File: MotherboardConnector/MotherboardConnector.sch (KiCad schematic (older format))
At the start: 2 parts

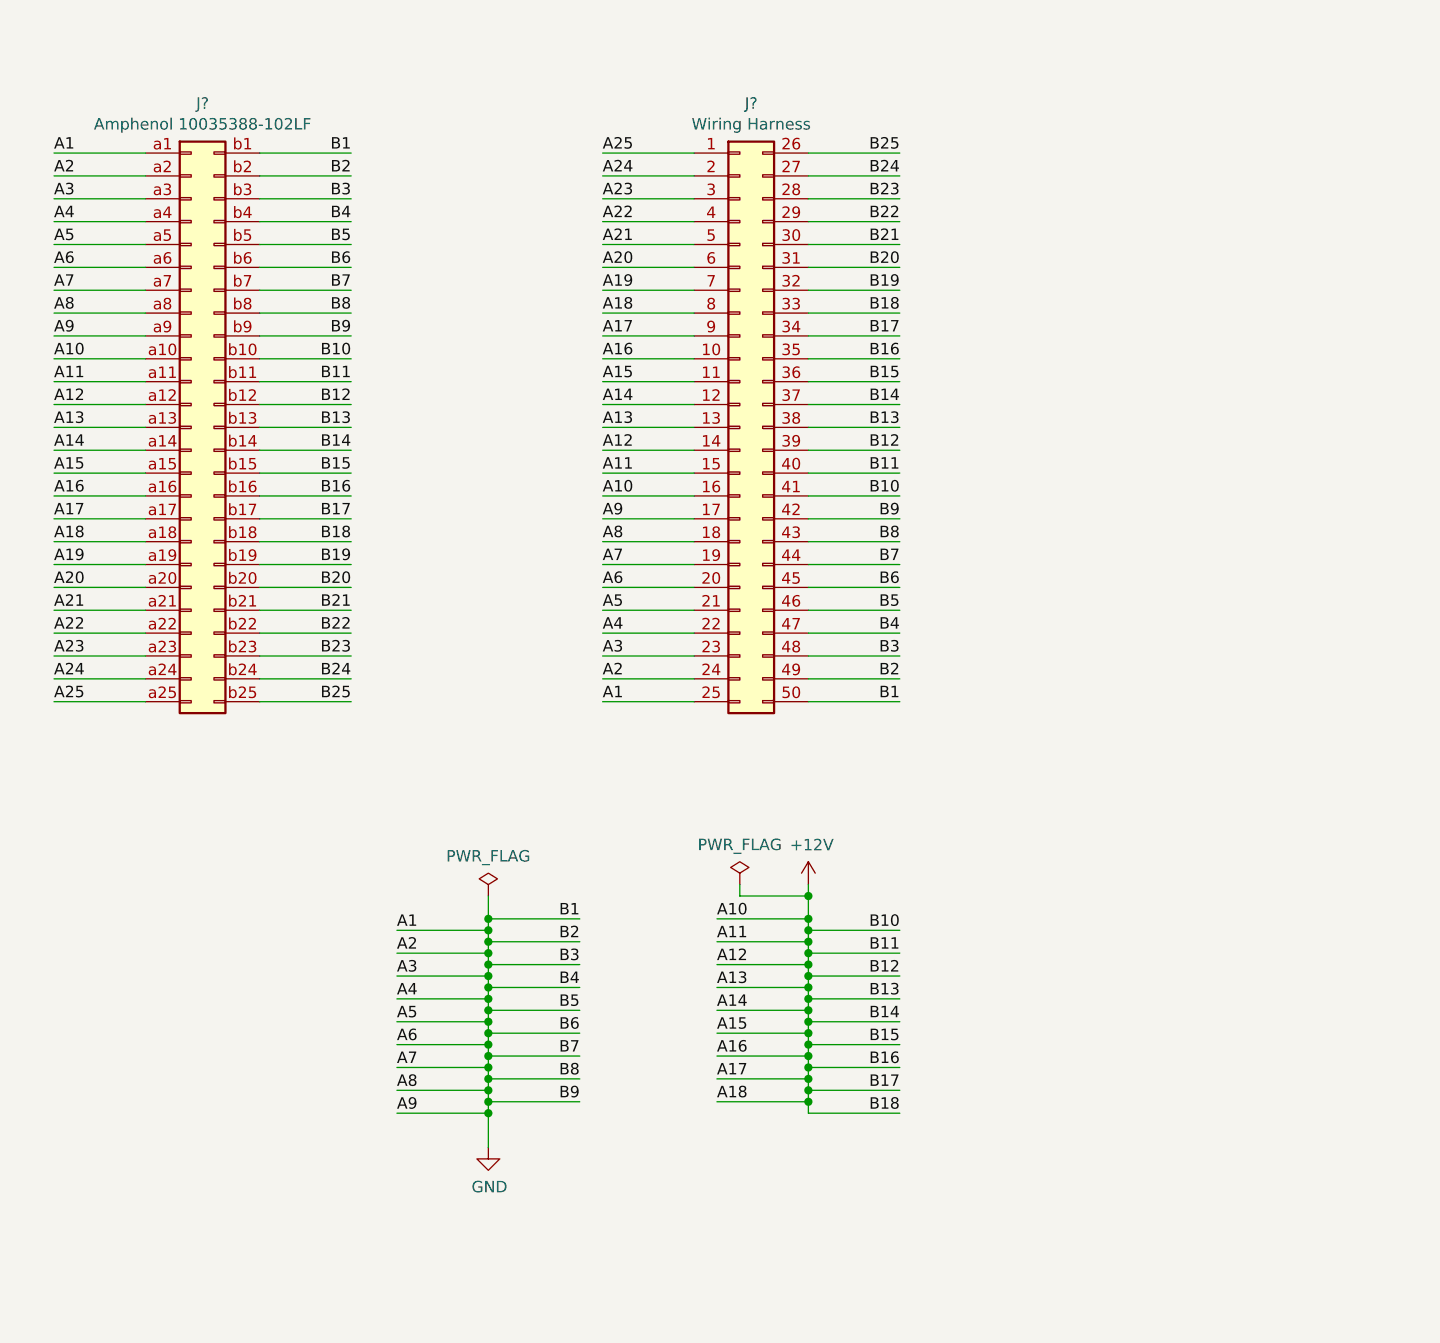
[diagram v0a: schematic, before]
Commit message: change to terminal block connector
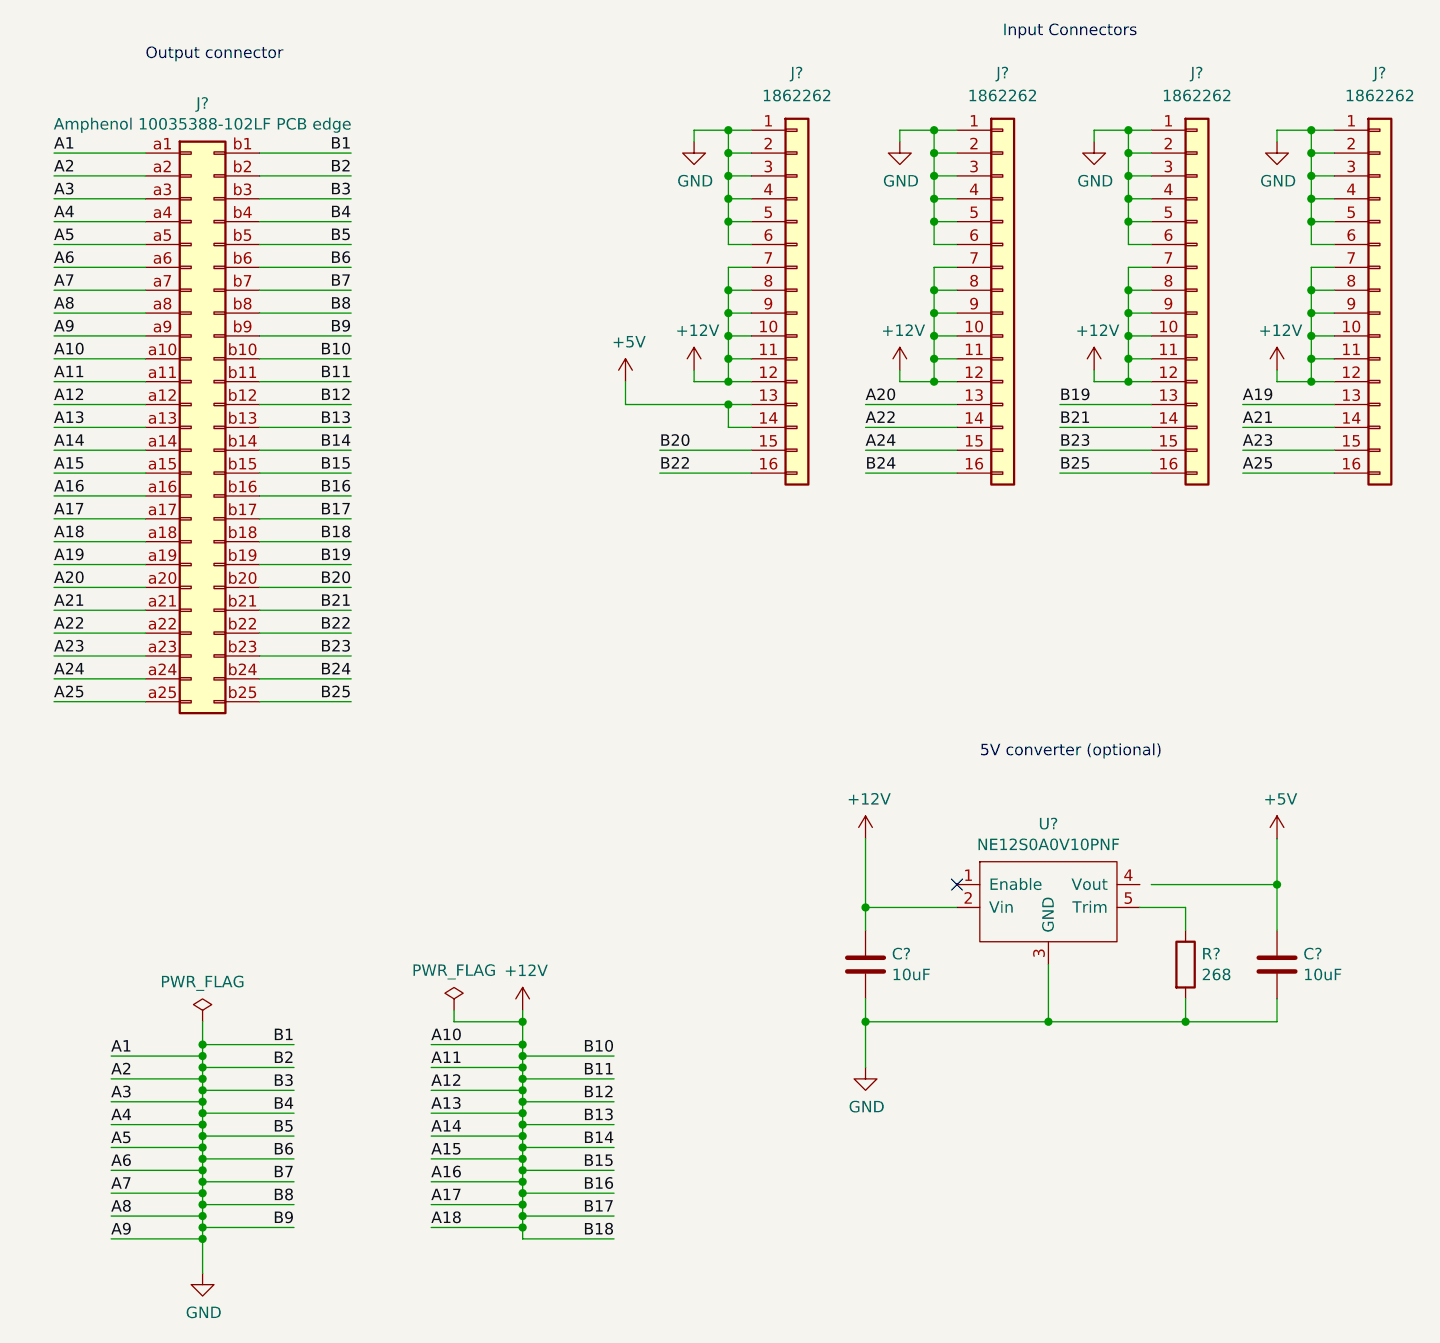
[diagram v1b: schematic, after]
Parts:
- removed J?: Amphenol 10035388-102LF, symbol Connector_Generic:Conn_02x25_Row_Letter_First
- removed J?: Wiring Harness, symbol Connector_Generic:Conn_02x25_Top_Bottom
- added C? (x2): 10uF, symbol Device:C
- added J? (x4): 1862262, symbol Connector_Generic:Conn_01x16
- added J?: Amphenol 10035388-102LF PCB edge, symbol Connector_Generic:Conn_02x25_Row_Letter_First
- added R?: 268, symbol Device:R
- added U?: NE12S0A0V10PNF, symbol NE12S0A0V10PNF:NE12S0A0V10PNF
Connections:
- net +12V: now also C?.1, J?.10 (Pin_10), J?.10 (Pin_10), J?.10 (Pin_10), J?.10 (Pin_10), J?.11 (Pin_11), J?.11 (Pin_11), J?.11 (Pin_11), J?.11 (Pin_11), J?.12 (Pin_12), J?.12 (Pin_12), J?.12 (Pin_12), J?.12 (Pin_12), J?.7 (Pin_7), J?.7 (Pin_7), J?.7 (Pin_7), J?.7 (Pin_7), J?.8 (Pin_8), J?.8 (Pin_8), J?.8 (Pin_8), J?.8 (Pin_8), J?.9 (Pin_9), J?.9 (Pin_9), J?.9 (Pin_9), J?.9 (Pin_9), J?.a10 (Pin_a10), J?.a11 (Pin_a11), J?.a12 (Pin_a12), J?.a13 (Pin_a13), J?.a14 (Pin_a14), J?.a15 (Pin_a15), J?.a16 (Pin_a16), J?.a17 (Pin_a17), J?.a18 (Pin_a18), J?.b10 (Pin_b10), J?.b11 (Pin_b11), J?.b12 (Pin_b12), J?.b13 (Pin_b13), J?.b14 (Pin_b14), J?.b15 (Pin_b15), J?.b16 (Pin_b16), J?.b17 (Pin_b17), J?.b18 (Pin_b18), U?.2 (Vin)
- net A19: now also J?.13 (Pin_13), J?.a19 (Pin_a19)
- net A20: now also J?.13 (Pin_13), J?.a20 (Pin_a20)
- net A21: now also J?.14 (Pin_14), J?.a21 (Pin_a21)
- net A22: now also J?.14 (Pin_14), J?.a22 (Pin_a22)
- net A23: now also J?.15 (Pin_15), J?.a23 (Pin_a23)
- net A24: now also J?.15 (Pin_15), J?.a24 (Pin_a24)
- net A25: now also J?.16 (Pin_16), J?.a25 (Pin_a25)
- net B19: now also J?.13 (Pin_13), J?.b19 (Pin_b19)
- net B20: now also J?.15 (Pin_15), J?.b20 (Pin_b20)
- net B21: now also J?.14 (Pin_14), J?.b21 (Pin_b21)
- net B22: now also J?.16 (Pin_16), J?.b22 (Pin_b22)
- net B23: now also J?.15 (Pin_15), J?.b23 (Pin_b23)
- net B24: now also J?.16 (Pin_16), J?.b24 (Pin_b24)
- net B25: now also J?.16 (Pin_16), J?.b25 (Pin_b25)
- net GND: now also C?.2, C?.2, J?.1 (Pin_1), J?.1 (Pin_1), J?.1 (Pin_1), J?.1 (Pin_1), J?.2 (Pin_2), J?.2 (Pin_2), J?.2 (Pin_2), J?.2 (Pin_2), J?.3 (Pin_3), J?.3 (Pin_3), J?.3 (Pin_3), J?.3 (Pin_3), J?.4 (Pin_4), J?.4 (Pin_4), J?.4 (Pin_4), J?.4 (Pin_4), J?.5 (Pin_5), J?.5 (Pin_5), J?.5 (Pin_5), J?.5 (Pin_5), J?.6 (Pin_6), J?.6 (Pin_6), J?.6 (Pin_6), J?.6 (Pin_6), J?.a1 (Pin_a1), J?.a2 (Pin_a2), J?.a3 (Pin_a3), J?.a4 (Pin_a4), J?.a5 (Pin_a5), J?.a6 (Pin_a6), J?.a7 (Pin_a7), J?.a8 (Pin_a8), J?.a9 (Pin_a9), J?.b1 (Pin_b1), J?.b2 (Pin_b2), J?.b3 (Pin_b3), J?.b4 (Pin_b4), J?.b5 (Pin_b5), J?.b6 (Pin_b6), J?.b7 (Pin_b7), J?.b8 (Pin_b8), J?.b9 (Pin_b9), R?.2, U?.3 (GND)
- new net: R?.1, U?.5 (Trim)
- new net +5V: C?.1, J?.13 (Pin_13), J?.14 (Pin_14)
- no-connect marks 0 -> 1
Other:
- note added: "5V converter (optional)"
- note added: "Input Connectors"
- note added: "Output connector"
